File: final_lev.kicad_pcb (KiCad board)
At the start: 2 copper layers, 160 x 140 mm, 184 parts, among them J101 +60V IN, J201 RAILS IN, J202 CONTROL, J203 YOKE 1, J204 YOKE 2, Q1 IRF100B201, Q2 IRF100B201, Q201 IRF100B201, Q202 IRF100B201, Q203 IRF100B201, Q204 IRF100B201, Q3 IRF100B201, Q4 IRF100B201, U1 IR2184, U2 IR2184, U201 74LVC2G17, U202 74LVC2G17, U203 INA240A2D, U204 LM2903B, U205 74HCT74, U206 IR2184, U207 IR2184, U208 74HCT132, U3 INA240A2D, U4 LM2903B, U5 74HCT74, U6 74HCT132

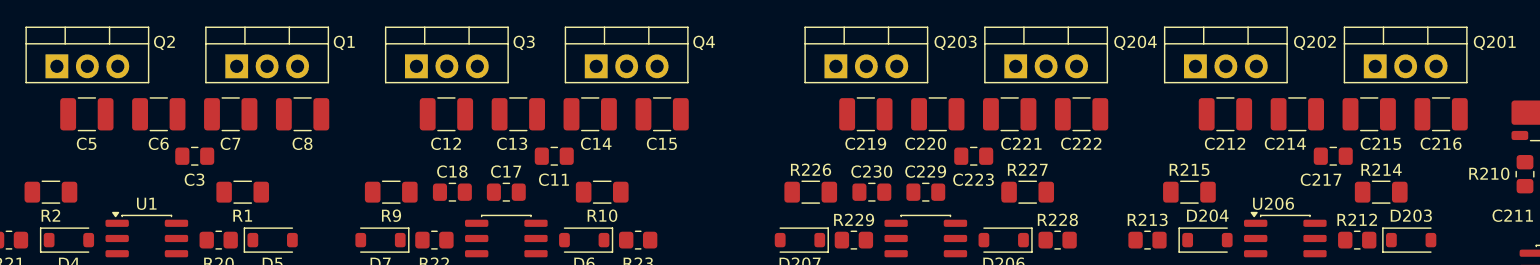
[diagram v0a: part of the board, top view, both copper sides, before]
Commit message: 4-layer stackup, net class split, DRC rules, leg-A ceramic rotation
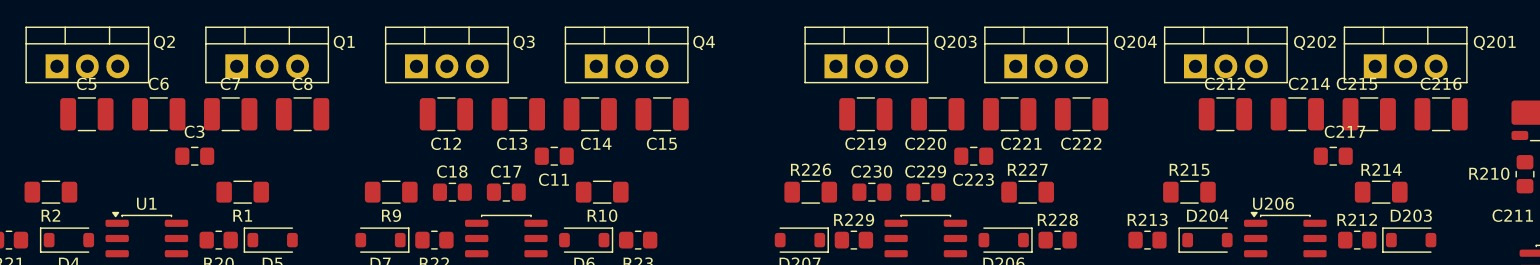
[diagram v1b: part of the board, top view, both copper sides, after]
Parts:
- turned C212 to 180 degrees
- turned C214 to 180 degrees
- turned C215 to 180 degrees
- turned C216 to 180 degrees
- turned C217 to 180 degrees
- turned C3 to 180 degrees
- turned C5 to 180 degrees
- turned C6 to 180 degrees
- turned C7 to 180 degrees
- turned C8 to 180 degrees
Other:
- copper layers 2 -> 4

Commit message: README with H-bridge sketch; In1.Cu ground plane; library mismatch investigation
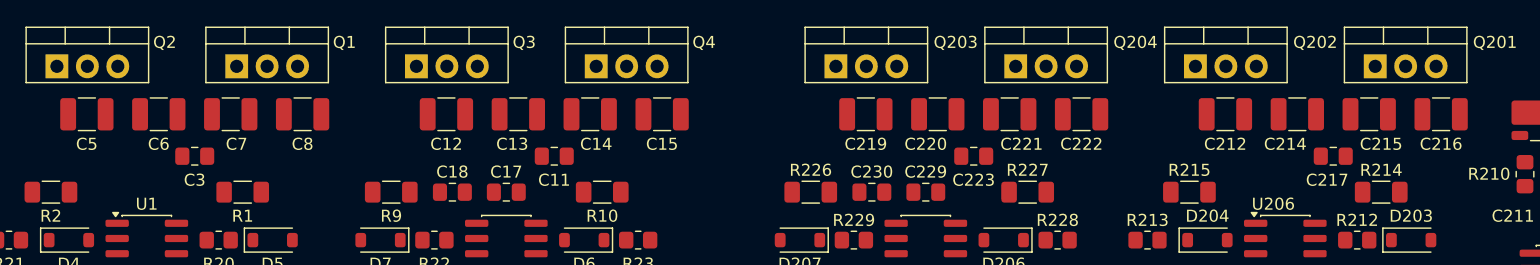
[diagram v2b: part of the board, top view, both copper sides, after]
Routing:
- added copper zone on In1.Cu, net GND
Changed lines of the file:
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@@
 		(tags "capacitor handsolder")
 		(property "Reference" "C212"
-			(at 0 2.5 180)
+			(at 0 -2.5 180)
 			(layer "F.SilkS")
 			(effects
@@
 		(tags "capacitor handsolder")
 		(property "Reference" "C5"
-			(at 0 2.5 180)
+			(at 0 -2.5 180)
 			(layer "F.SilkS")
 			(effects
@@
 		(tags "capacitor handsolder")
 		(property "Reference" "C217"
-			(at -1 2 180)
+			(at 0.5 -2 180)
 			(layer "F.SilkS")
 			(effects
@@
 		(tags "capacitor handsolder")
 		(property "Reference" "C216"
-			(at 0 2.5 180)
+			(at 0 -2.5 180)
 			(layer "F.SilkS")
 			(effects
@@
 		(tags "capacitor handsolder")
 		(property "Reference" "C8"
-			(at 0 2.5 180)
+			(at 0 -2.5 180)
 			(layer "F.SilkS")
 			(effects
@@
 		(tags "capacitor handsolder")
 		(property "Reference" "C3"
-			(at 0 2 180)
+			(at 0 -2 180)
 			(layer "F.SilkS")
 			(effects
@@
 		(tags "capacitor handsolder")
 		(property "Reference" "C7"
-			(at 0 2.5 180)
+			(at -0.5 -2.5 180)
 			(layer "F.SilkS")
 			(effects
@@
 		(tags "capacitor handsolder")
 		(property "Reference" "C215"
-			(at 1 2.5 180)
+			(at -1 -2.5 180)
 			(layer "F.SilkS")
 			(effects
@@
 		(tags "capacitor handsolder")
 		(property "Reference" "C214"
-			(at -1 2.5 180)
+			(at 1 -2.5 180)
 			(layer "F.SilkS")
 			(effects
@@
 		(tags "capacitor handsolder")
 		(property "Reference" "C6"
-			(at 0 2.5 180)
+			(at 0 -2.5 180)
 			(layer "F.SilkS")
 			(effects
@@
 		(layer "Edge.Cuts")
 	)
+	(zone
+		(net "GND")
+		(layer "In1.Cu")
+		(name "GND_PLANE_In1")
+		(hatch edge 0.5)
+		(connect_pads yes
+			(clearance 0.3)
+		)
+		(min_thickness 0.25)
+		(fill yes
+			(thermal_gap 0.5)
+			(thermal_bridge_width 0.5)
+			(island_removal_mode 0)
+		)
+		(polygon
+			(pts
+				(xy 100 50) (xy 260 50) (xy 260 190) (xy 100 190)
+			)
+		)
+	)
 	(embedded_fonts no)

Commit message: Placement review: 16 parts moved, lay.py placement checks, coil pours to B.Cu
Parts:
- moved R238 62.0 mm to (182.0, 97.5)
- moved C20 57.1 mm to (114.2, 80.5), turned to -90 degrees
- moved C213 39.8 mm to (245.8, 78.5), turned to 90 degrees
- moved C210 30.6 mm to (167.6, 172.6), turned to 180 degrees
- moved C209 20.6 mm to (171.7, 172.8)
- moved C237 15.5 mm to (222.7, 110.7), turned to 270 degrees
- moved C26 15.1 mm to (125.2, 112.7)
- moved C211 10.0 mm to (250.5, 84.5)
- moved C239 8.89 mm to (214.6, 106.8), turned to 180 degrees
- moved C2 8.13 mm to (138.2, 78.9)
- moved C228 8.13 mm to (233.2, 78.9)
- moved C27 7.85 mm to (115.7, 108.8)
- moved C25 3.78 mm to (115.8, 112.7)
- moved C235 3.51 mm to (213.3, 110.7), turned to 270 degrees
- moved C1 3.32 mm to (132.8, 81.7), turned to -90 degrees
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
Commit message: Coil pours, test points, and a pad-rotation defect found by tooling
Board:

- 13 test points placed, grounds first so every signal point sits within 7.5 mm of its own ground return

- All four 30 A coil pours drawn on B.Cu, single polygons, 10.7-11.0 mm at the narrowest cut

- 34 vias transitioning the two A legs from the surface-mount shunts down to B.Cu, 15 at 2.0 A on CH1 and 19 at 1.58 A on CH2

- The B legs need no vias: every pad carrying their current is through-hole

Fixed:

- 20 footprints had pads that did not follow their body rotation, 5 of them off by 90 degrees, which turns a 1.175 x 1.450 mm pad across the part instead of along it. Repaired by Update Footprints from Library

- A12 corrected twice. The mounting holes are plated M3 pads on all four layers with no net, not the unplated holes I first reported

Tools:

- pour_check.py rasterises pour outlines at 0.05 mm; lay.py's bounding-box zone check was blind to polygons and missed a 6.5 mm band that needed 10.7

- lay.py gained pad-rotation and zone-priority checks, both regression tested against the broken versions
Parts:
- added TP201: TestPoint, TestPoint:TestPoint_Loop_D2.50mm_Drill1.0mm, F.Cu at (116.8, 120.2)
- added TP202: TestPoint, TestPoint:TestPoint_Loop_D2.50mm_Drill1.0mm, F.Cu at (214.2, 118.8)
- added TP203: TestPoint, TestPoint:TestPoint_Loop_D2.50mm_Drill1.0mm, F.Cu at (120.5, 121.7)
- added TP204: TestPoint, TestPoint:TestPoint_Loop_D2.50mm_Drill1.0mm, F.Cu at (210.7, 116.0)
- added TP205: TestPoint, TestPoint:TestPoint_Loop_D2.50mm_Drill1.0mm, F.Cu at (124.2, 116.4)
- added TP206: TestPoint, TestPoint:TestPoint_Loop_D2.50mm_Drill1.0mm, F.Cu at (210.3, 112.4)
- added TP207: TestPoint, TestPoint:TestPoint_Loop_D2.50mm_Drill1.0mm, F.Cu at (116.8, 116.4)
- added TP208: TestPoint, TestPoint:TestPoint_Loop_D2.50mm_Drill1.0mm, F.Cu at (214.2, 115.1)
- added TP209: TestPoint, TestPoint:TestPoint_Loop_D2.50mm_Drill1.0mm, F.Cu at (203.6, 174.7)
- added TP210: TestPoint, TestPoint:TestPoint_Loop_D2.50mm_Drill1.0mm, F.Cu at (196.1, 174.7)
- added TP211: TestPoint, TestPoint:TestPoint_Loop_D2.50mm_Drill1.0mm, F.Cu at (198.8, 171.1)
- added TP212: TestPoint, TestPoint:TestPoint_Loop_D2.50mm_Drill1.0mm, F.Cu at (199.8, 174.7)
- added TP213: TestPoint, TestPoint:TestPoint_Loop_D2.50mm_Drill1.0mm, F.Cu at (183.2, 70.0)
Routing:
- net /COIL_A2: vias 0 -> 19
- net /COIL_A1: vias 0 -> 15
- added copper zone on B.Cu, net /COIL_A1
- added copper zone on F.Cu, net /COIL_A1
- added copper zone on B.Cu, net /COIL_A2
- added copper zone on F.Cu, net /COIL_A2
- added copper zone on B.Cu, net /COIL_B1
- added copper zone on B.Cu, net /COIL_B2

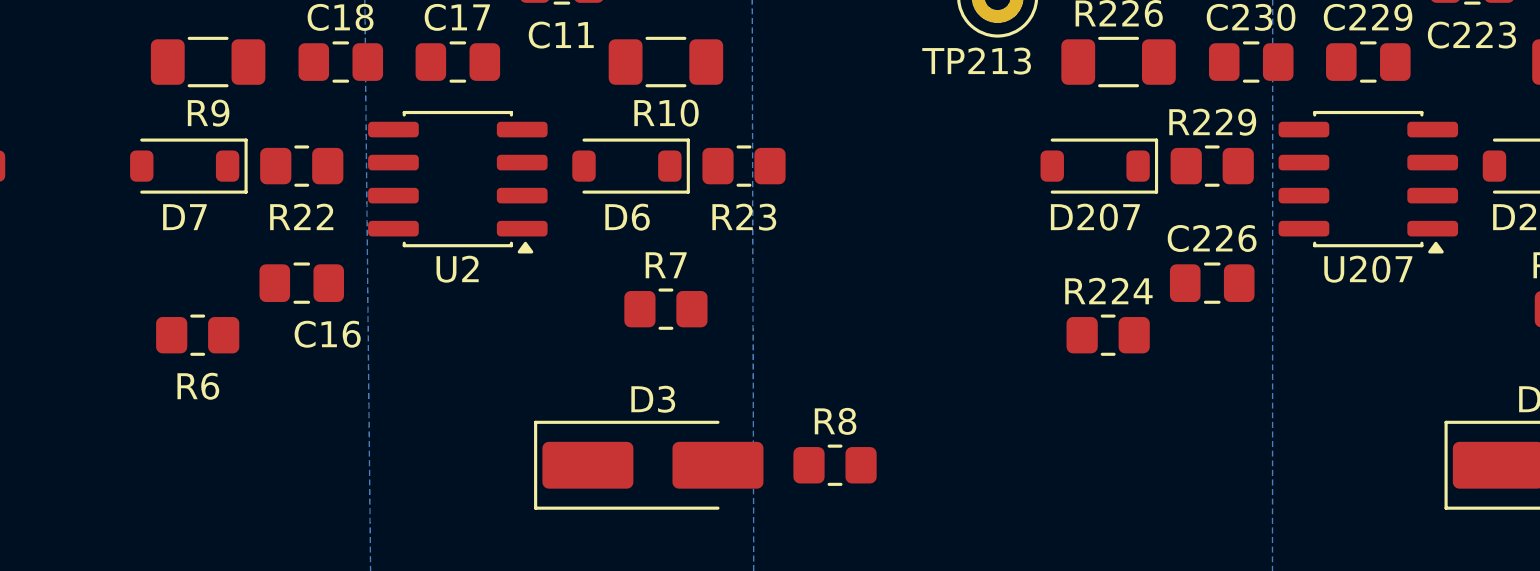
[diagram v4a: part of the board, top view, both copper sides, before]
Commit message: Complete the four coil nets: gate-drive stubs, VS vias, and drop the DRC rule that could not do its job
- Six gate-drive connections routed on F.Cu: driver VS, bootstrap return and gate-source resistor on each channel

- R6 and R224 rotated 180 so the coil pad faces the run, cutting each stub from 27.6 mm to 15.3 mm

- Two vias per channel tying each stub to its B.Cu pour. The stub is front copper and the pour is back copper; a shared net name is not a connection

- Removed the HV_POWER 10.7 mm track_width rule. It matched GND and every gate-drive net, so it demanded 10.7 mm for a bootstrap cap hop. Pour width is now verified by tools/pour_check.py, which can actually see a zone
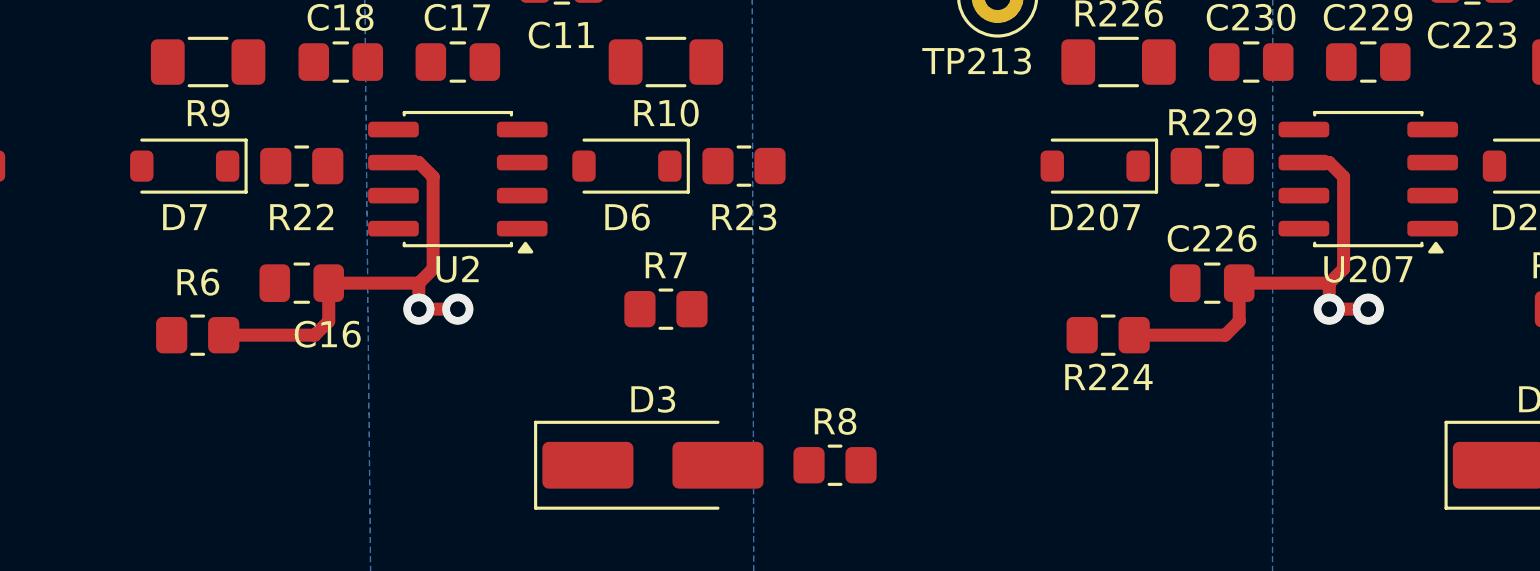
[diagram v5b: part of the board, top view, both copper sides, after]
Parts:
- turned R224 to 180 degrees
- turned R6 to 180 degrees
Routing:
- net /COIL_B2: track 0.00 -> 17.8 mm, vias 0 -> 2
- net /COIL_B1: track 0.00 -> 17.8 mm, vias 0 -> 2
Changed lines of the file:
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@@
 	(footprint "Resistor_SMD:R_0805_2012Metric_Pad1.20x1.40mm_HandSolder"
 		(layer "F.Cu")
-		(at 187.5 83)
+		(at 187.5 83 180)
 		(descr "Resistor SMD 0805 (2012 Metric), square (rectangular) end terminal, IPC-7351 nominal with elongated pad for handsoldering. (Body size source: IPC-SM-782 page 72, https://www.pcb-3d.com/wordpress/wp-content/uploads/ipc-sm-782a_amendment_1_and_2.pdf)")
 		(tags "resistor handsolder")
@@
 		(duplicate_pad_numbers_are_jumpers no)
 		(fp_line
-			(start -0.227064 -0.735)
-			(end 0.227064 -0.735)
+			(start -0.227064 0.735)
+			(end 0.227064 0.735)
 			(stroke
 				(width 0.12)
@@
 		)
 		(fp_line
-			(start -0.227064 0.735)
-			(end 0.227064 0.735)
+			(start -0.227064 -0.735)
+			(end 0.227064 -0.735)
 			(stroke
 				(width 0.12)
@@
 		)
 		(pad "1" smd roundrect
-			(at -1 0)
+			(at -1 0 180)
 			(size 1.2 1.4)
 			(layers "F.Cu" "F.Mask" "F.Paste")
@@
 		)
 		(pad "2" smd roundrect
-			(at 1 0)
+			(at 1 0 180)
 			(size 1.2 1.4)
 			(layers "F.Cu" "F.Mask" "F.Paste")
@@
 	(footprint "Resistor_SMD:R_0805_2012Metric_Pad1.20x1.40mm_HandSolder"
 		(layer "F.Cu")
-		(at 152.5 83)
+		(at 152.5 83 180)
 		(descr "Resistor SMD 0805 (2012 Metric), square (rectangular) end terminal, IPC-7351 nominal with elongated pad for handsoldering. (Body size source: IPC-SM-782 page 72, https://www.pcb-3d.com/wordpress/wp-content/uploads/ipc-sm-782a_amendment_1_and_2.pdf)")
 		(tags "resistor handsolder")
@@
 		(duplicate_pad_numbers_are_jumpers no)
 		(fp_line
-			(start -0.227064 -0.735)
-			(end 0.227064 -0.735)
+			(start -0.227064 0.735)
+			(end 0.227064 0.735)
 			(stroke
 				(width 0.12)
@@
 		)
 		(fp_line
-			(start -0.227064 0.735)
-			(end 0.227064 0.735)
+			(start -0.227064 -0.735)
+			(end 0.227064 -0.735)
 			(stroke
 				(width 0.12)
@@
 		)
 		(pad "1" smd roundrect
-			(at -1 0)
+			(at -1 0 180)
 			(size 1.2 1.4)
 			(layers "F.Cu" "F.Mask" "F.Paste")
@@
 		)
 		(pad "2" smd roundrect
-			(at 1 0)
+			(at 1 0 180)
 			(size 1.2 1.4)
 			(layers "F.Cu" "F.Mask" "F.Paste")
@@
 		(layer "Edge.Cuts")
 	)
+	(segment
+		(start 161.55 76.915001)
+		(end 161.55 80.45)
+		(width 0.5)
+		(layer "F.Cu")
+		(net "/COIL_B1")
+	)
+	(segment
+		(start 161 81)
+		(end 157.5375 81)
+		(width 0.5)
+		(layer "F.Cu")
+		(net "/COIL_B1")
+	)
+	(segment
+		(start 161 81)
+		(end 161 82)
+		(width 0.5)
+		(layer "F.Cu")
+		(net "/COIL_B1")
+	)
+	(segment
+		(start 160.999999 76.365)
+		(end 161.55 76.915001)
+		(width 0.5)
+		(layer "F.Cu")
+		(net "/COIL_B1")
+	)
+	(segment
+		(start 161.55 80.45)
+		(end 161 81)
+		(width 0.5)
+		(layer "F.Cu")
+		(net "/COIL_B1")
+	)
+	(segment
+		(start 161 82)
+		(end 162.5 82)
+		(width 0.5)
+		(layer "F.Cu")
+		(net "/COIL_B1")
+	)
+	(segment
+		(start 153.5 83)
+		(end 157 83)
+		(width 0.5)
+		(layer "F.Cu")
+		(net "/COIL_B1")
+	)
+	(segment
+		(start 157.5375 82.4625)
+		(end 157.5375 81)
+		(width 0.5)
+		(layer "F.Cu")
+		(net "/COIL_B1")
+	)
+	(segment
+		(start 157 83)
+		(end 157.5375 82.4625)
+		(width 0.5)
+		(layer "F.Cu")
+		(net "/COIL_B1")
+	)
+	(segment
+		(start 160.025 76.365)
+		(end 160.999999 76.365)
+		(width 0.5)
+		(layer "F.Cu")
+		(net "/COIL_B1")
+	)
+	(via
+		(at 161 82)
+		(size 1.2)
+		(drill 0.6)
+		(layers "F.Cu" "B.Cu")
+		(net "/COIL_B1")
+	)
+	(via
+		(at 162.5 82)
+		(size 1.2)
+		(drill 0.6)
+		(layers "F.Cu" "B.Cu")
+		(net "/COIL_B1")
+	)
+	(segment
+		(start 196 81)
+		(end 192.5375 81)
+		(width 0.5)
+		(layer "F.Cu")
+		(net "/COIL_B2")
+	)
+	(segment
+		(start 196.55 80.45)
+		(end 196 81)
+		(width 0.5)
+		(layer "F.Cu")
+		(net "/COIL_B2")
+	)
+	(segment
+		(start 195.999999 76.365)
+		(end 196.55 76.915001)
+		(width 0.5)
+		(layer "F.Cu")
+		(net "/COIL_B2")
+	)
+	(segment
+		(start 196 82)
+		(end 197.5 82)
+		(width 0.5)
+		(layer "F.Cu")
+		(net "/COIL_B2")
+	)
+	(segment
+		(start 192 83)
+		(end 192.5375 82.4625)
+		(width 0.5)
+		(layer "F.Cu")
+		(net "/COIL_B2")
+	)
+	(segment
+		(start 195.025 76.365)
+		(end 195.999999 76.365)
+		(width 0.5)
+		(layer "F.Cu")
+		(net "/COIL_B2")
+	)
+	(segment
+		(start 196.55 76.915001)
+		(end 196.55 80.45)
+		(width 0.5)
+		(layer "F.Cu")
+		(net "/COIL_B2")
+	)
+	(segment
+		(start 196 81)
+		(end 196 82)
+		(width 0.5)
+		(layer "F.Cu")
+		(net "/COIL_B2")
+	)
+	(segment
+		(start 192.5375 82.4625)
+		(end 192.5375 81)
+		(width 0.5)
+		(layer "F.Cu")
+		(net "/COIL_B2")
+	)
+	(segment
+		(start 188.5 83)
+		(end 192 83)
+		(width 0.5)
+		(layer "F.Cu")
+		(net "/COIL_B2")
+	)
+	(via
+		(at 196 82)
+		(size 1.2)
+		(drill 0.6)
+		(layers "F.Cu" "B.Cu")
+		(net "/COIL_B2")
+	)
+	(via
+		(at 197.5 82)
+		(size 1.2)
+		(drill 0.6)
+		(layers "F.Cu" "B.Cu")
+		(net "/COIL_B2")
+	)
 	(via

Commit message: In2.Cu power plane, and A17 recomputed as a plane instead of a trace
- +60V plane on In2.Cu with a finger to J101; reaches all 11 current-carrying pads through their own barrels, no vias in the power path

- In2 split: GND below y=150 either side of the finger, so the IO connector signals on B.Cu have a ground reference rather than the bus

- A17 corrected. The 28.0 mm figure applied the IPC-2221 trace formula to a plane; the same formula wants 146 mm on 1 oz inner, which is wider than the board. As a plane it is 0.54 squares, 0.46 mOhm end to end, 27 mV and 1.65 W at 60 A

- lay.py zone overlap now rasterises outlines; bounding boxes reported two false collisions against the L-shaped plane
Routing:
- added copper zone on In2.Cu, net +60V
- added copper zone on In2.Cu, net GND
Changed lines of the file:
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@@
+		)
+	)
+	(zone
+		(net "+60V")
+		(layer "In2.Cu")
+		(name "PLUS60V_PLANE_In2")
+		(hatch edge 0.5)
+		(priority 6)
+		(connect_pads yes
+			(clearance 0.3)
+		)
+		(min_thickness 0.25)
+		(fill yes
+			(thermal_gap 0.5)
+			(thermal_bridge_width 0.5)
+			(island_removal_mode 0)
+		)
+		(polygon
+			(pts
+				(xy 100 50) (xy 260 50) (xy 260 150) (xy 162 150) (xy 162 188) (xy 146 188) (xy 146 150) (xy 100 150)
+			)
+		)
+	)
+	(zone
+		(net "GND")
+		(layer "In2.Cu")
+		(name "GND_In2_right")
+		(hatch edge 0.5)
+		(priority 8)
+		(connect_pads yes
+			(clearance 0.3)
+		)
+		(min_thickness 0.25)
+		(fill yes
+			(thermal_gap 0.5)
+			(thermal_bridge_width 0.5)
+			(island_removal_mode 0)
+		)
+		(polygon
+			(pts
+				(xy 165 152) (xy 260 152) (xy 260 188) (xy 165 188)
+			)
+		)
+	)
+	(zone
+		(net "GND")
+		(layer "In2.Cu")
+		(name "GND_In2_left")
+		(hatch edge 0.5)
+		(priority 7)
+		(connect_pads yes
+			(clearance 0.3)
+		)
+		(min_thickness 0.25)
+		(fill yes
+			(thermal_gap 0.5)
+			(thermal_bridge_width 0.5)
+			(island_removal_mode 0)
+		)
+		(polygon
+			(pts
+				(xy 100 152) (xy 144 152) (xy 144 188) (xy 100 188)
+			)
 		)
 	)
